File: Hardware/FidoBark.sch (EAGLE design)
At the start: 27 parts, among them IC1 STM32F405RGT, J4 MICRO-SDCARD-CONNECTOR-330006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, U1 IP4220CZ6, Y1_8MHZ 631-1100-ND, Y2_32.768KHZ 32.768KHz

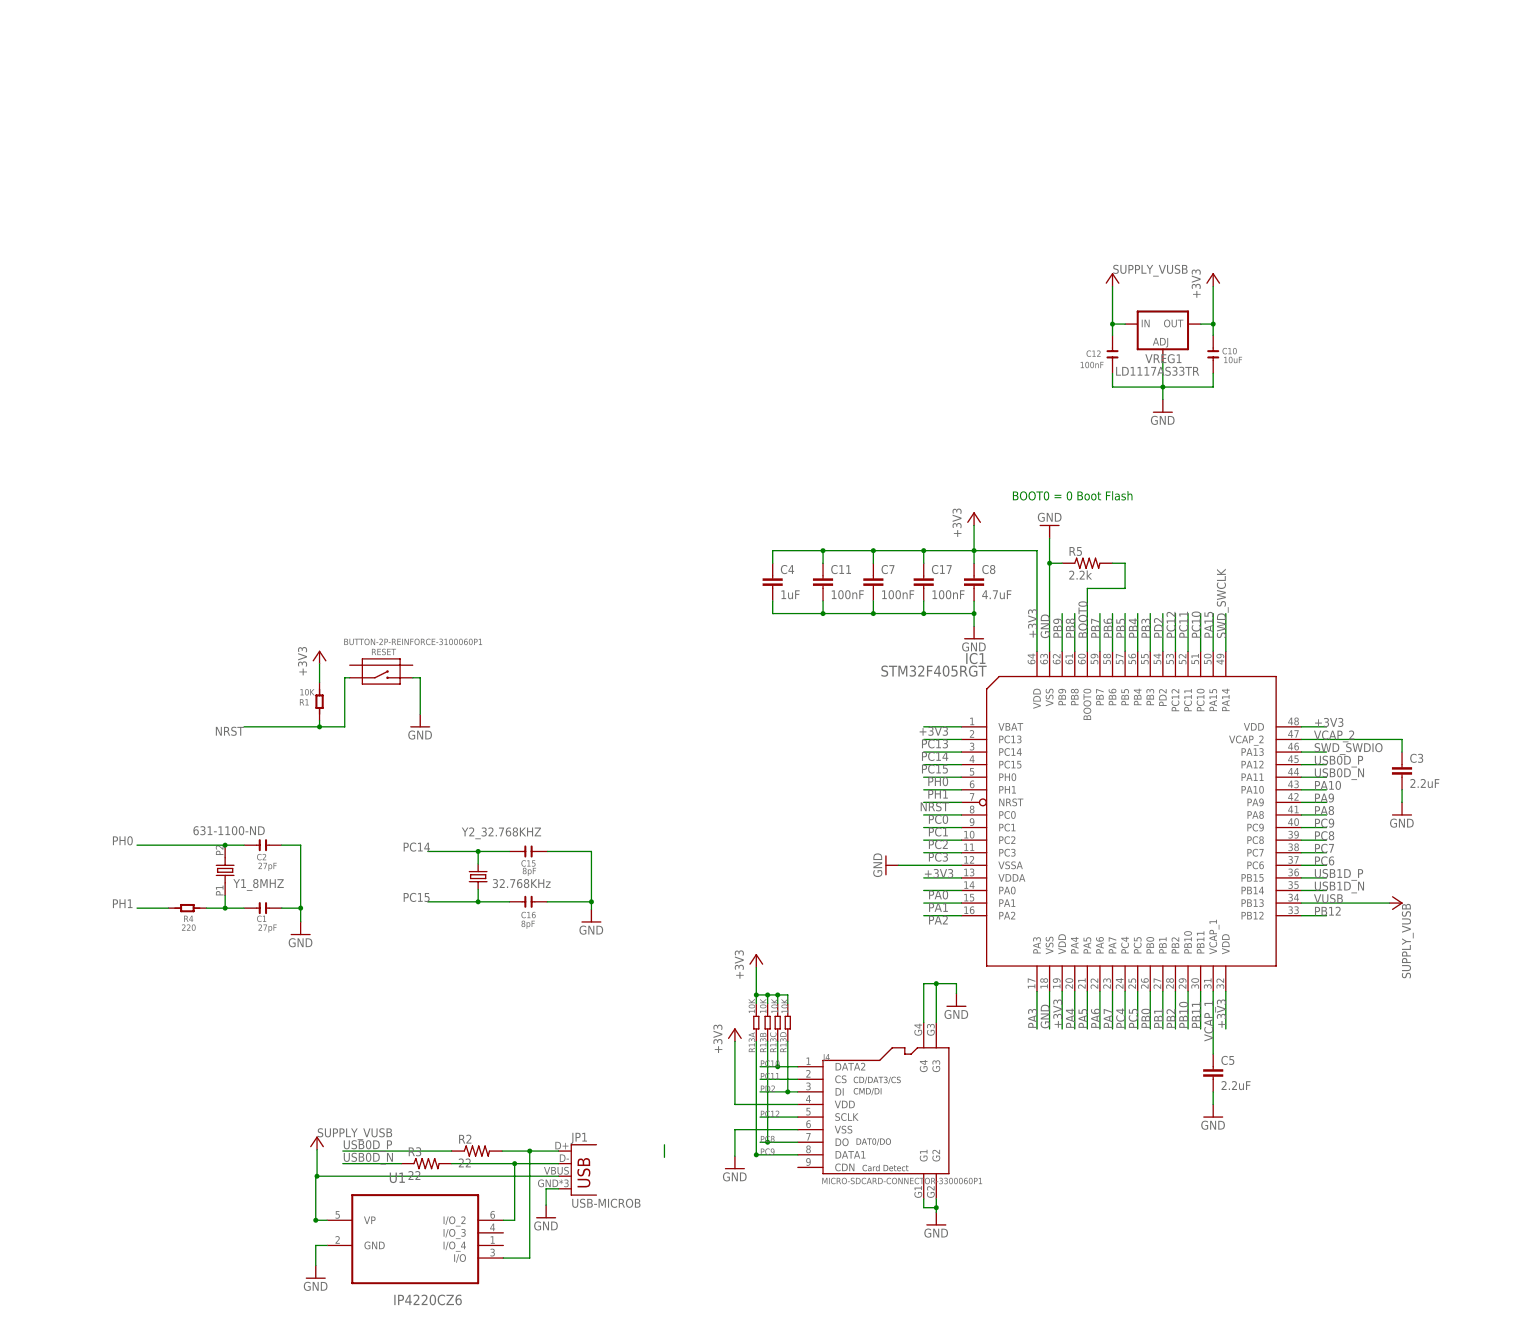
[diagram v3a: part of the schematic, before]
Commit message: power, micro controller, USB, and microsd
I’m considering making a dev board just for this
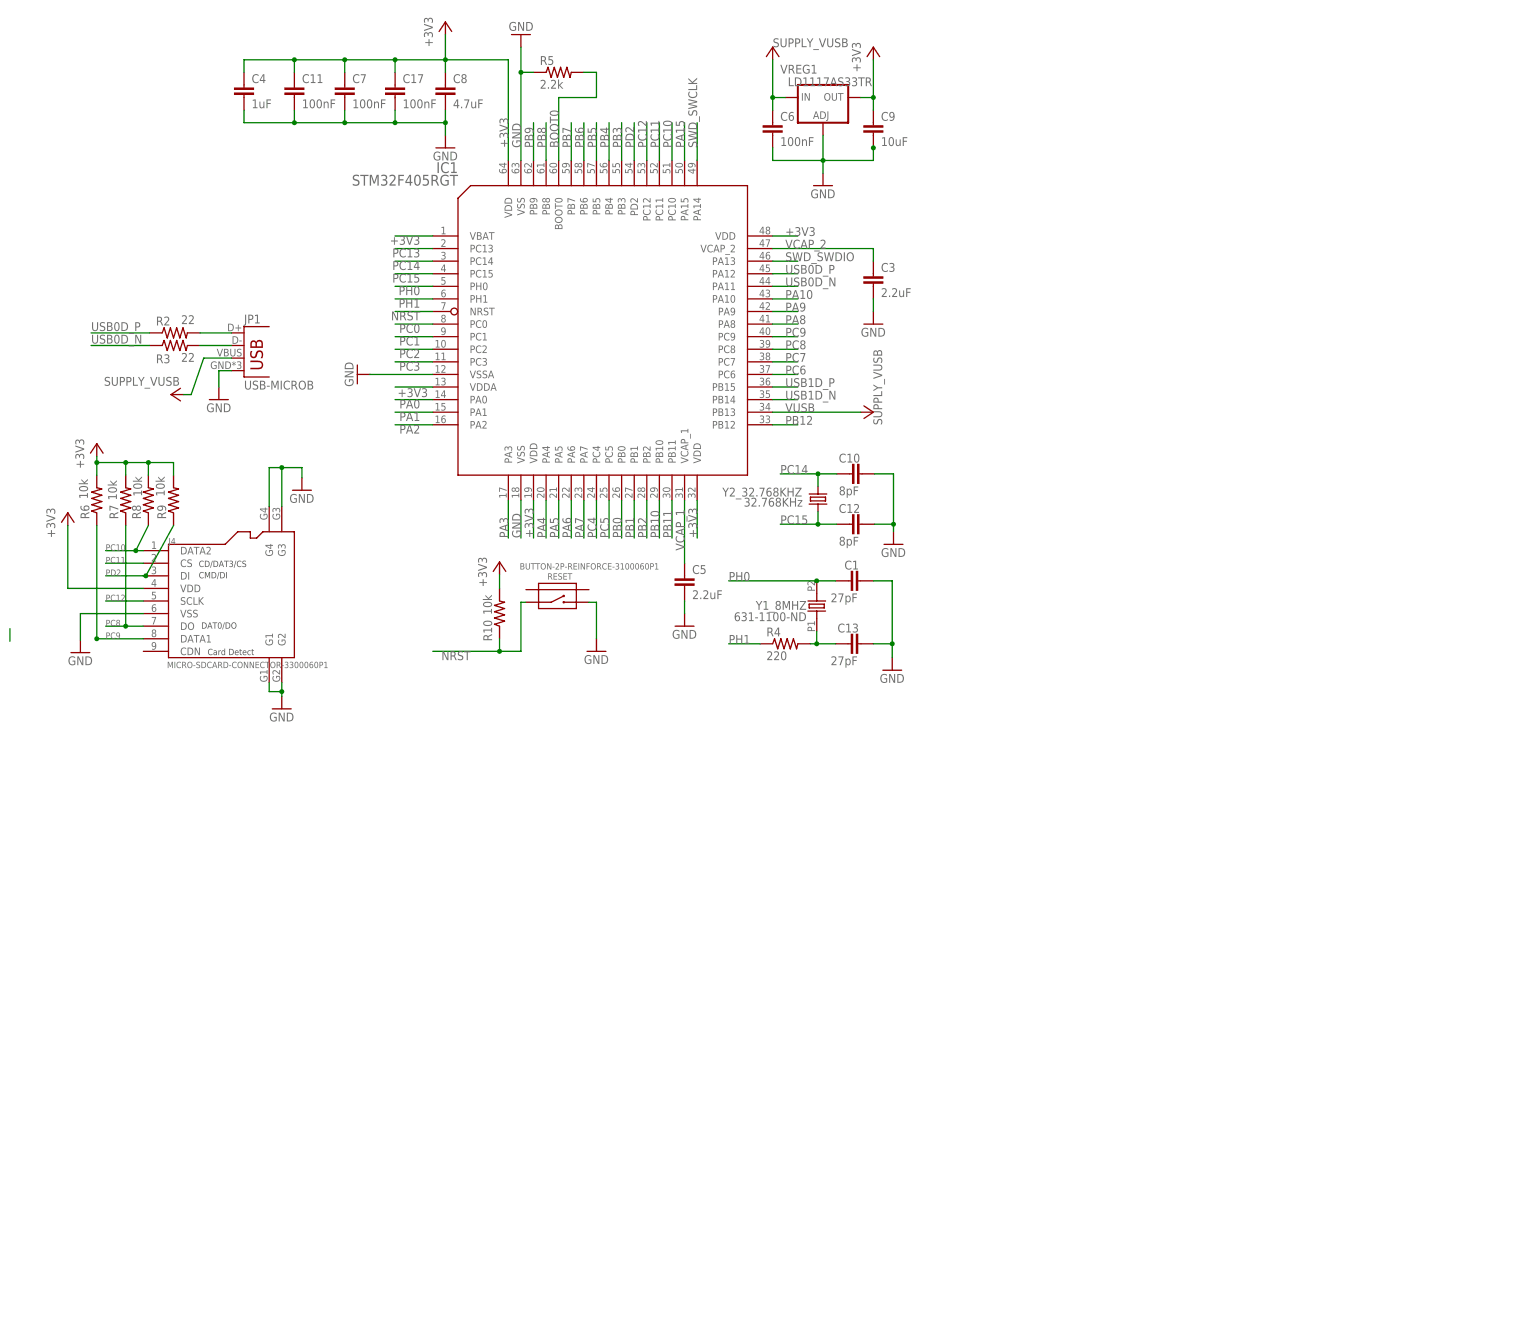
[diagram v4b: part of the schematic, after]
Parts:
- removed C15, C16: 8pF, OPL:C-0603
- removed C2: 27pF, OPL:C-0603
- removed R1: 10K, OPL:R-0603
- removed R13: 10K, OPL:R-4R
- removed U1: IP4220CZ6, 0ben:IP4220CZ6
- added C13: 27pF, rcl:C-EUC0603
- added C6: 100nF, rcl:C-EUC0603
- added C9: 10uF, rcl:C-EUC0603
- added R10, R6, R7, R8, R9: 10k, rcl:R-US_R0603
- C1: device OPL:C-0603 -> rcl:C-EUC0603
- C10: value 10uF -> 8pF; device OPL:C-0805 -> rcl:C-EUC0603
- C12: value 100nF -> 8pF; device OPL:C-0603 -> rcl:C-EUC0603
- R4: device OPL:R-0603 -> rcl:R-US_R0603
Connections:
- net +3V3: now also C9.1, R10.2, R6.2, R7.2, R8.2, R9.2; no longer C10.1, R1.2, R13A.2, R13B.2, R13C.2, R13D.2
- net GND: now also C13.2, C5.2, C6.2, C9.2; no longer C15.2, C16.2, C2.2, U1.GND
- net N$1: now also C13.1, R4.2; no longer C1.1, R4.1
- net NRST: now also R10.1; no longer R1.1
- net PC10: now also R8.1; no longer R13C.1
- net PC14: now also C10.1; no longer C15.1
- net PC15: now also C12.1; no longer C16.1
- net PC8: now also R7.1; no longer R13B.1
- net PC9: now also R6.1; no longer R13A.1
- net PD2: now also R9.1; no longer R13D.1
- net PH0: now also C1.1; no longer C2.1
- net PH1: now also R4.1; no longer R4.2
- net USB0_D+: no longer U1.I/O
- net USB0_D-: no longer U1.I/O_2
- net VUSB: now also C6.1; no longer C12.1, U1.VP
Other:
- note removed: "BOOT0 = 0 Boot Flash"
- moved on the sheet: C11, C17, C3, C4, C5, C7, C8, IC1, J4, JP1, R2, R3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

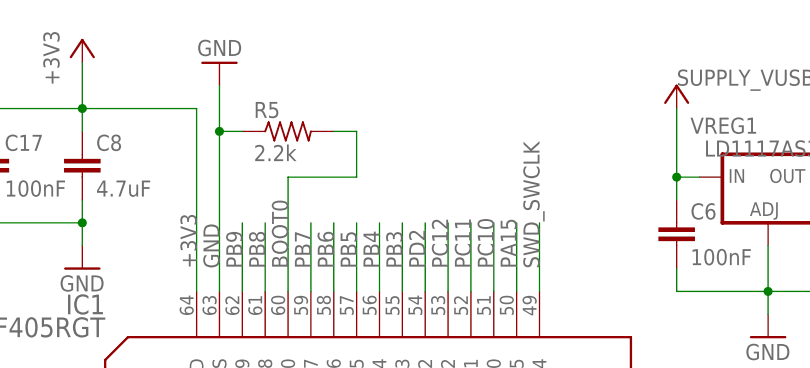
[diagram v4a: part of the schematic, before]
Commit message: added a programming jumper
kinda could be important
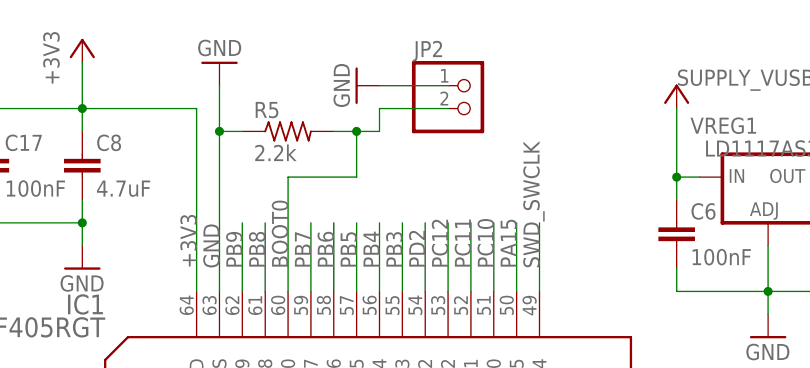
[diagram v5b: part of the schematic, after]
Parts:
- added JP2: (no value), pinhead:PINHD-1X2
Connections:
- net BOOT0: now also JP2.2
- net GND: now also JP2.1
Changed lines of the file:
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@@
 <part name="FRAME1" library="frames" deviceset="LETTER_P" device=""/>
 <part name="VUSB1" library="dp_devices" deviceset="SUPPLY_VUSB" device=""/>
+<part name="JP2" library="pinhead" deviceset="PINHD-1X2" device=""/>
+<part name="GND6" library="supply1" deviceset="GND" device=""/>
 </parts>
 <sheets>
@@
 <attribute name="VALUE" x="35.306" y="174.752" size="1.778" layer="96" rot="R180"/>
 </instance>
+<instance part="JP2" gate="G$1" x="132.08" y="238.76"/>
+<instance part="GND6" gate="1" x="119.38" y="241.3" rot="R270"/>
 </instances>
 <busses>
@@
 <wire x1="43.18" y1="176.022" x2="43.18" y2="172.72" width="0.1524" layer="91"/>
 </segment>
+<segment>
+<pinref part="JP2" gate="G$1" pin="1"/>
+<pinref part="GND6" gate="1" pin="GND"/>
+<wire x1="129.54" y1="241.3" x2="121.92" y2="241.3" width="0.1524" layer="91"/>
+</segment>
 </net>
 <net name="SWD_SWDIO" class="0">
@@
 <pinref part="R5" gate="G$1" pin="2"/>
 <wire x1="119.38" y1="236.22" x2="116.84" y2="236.22" width="0.1524" layer="91"/>
-</segment>
-</net>
+<wire x1="119.38" y1="236.22" x2="121.92" y2="236.22" width="0.1524" layer="91"/>
+<wire x1="121.92" y1="236.22" x2="121.92" y2="238.76" width="0.1524" layer="91"/>
+<junction x="119.38" y="236.22"/>
+<pinref part="JP2" gate="G$1" pin="2"/>
+<wire x1="121.92" y1="238.76" x2="129.54" y2="238.76" width="0.1524" layer="91"/>
+</segment>
+</net>
